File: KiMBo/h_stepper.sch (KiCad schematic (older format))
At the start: 24 parts, among them U18 TMC2130

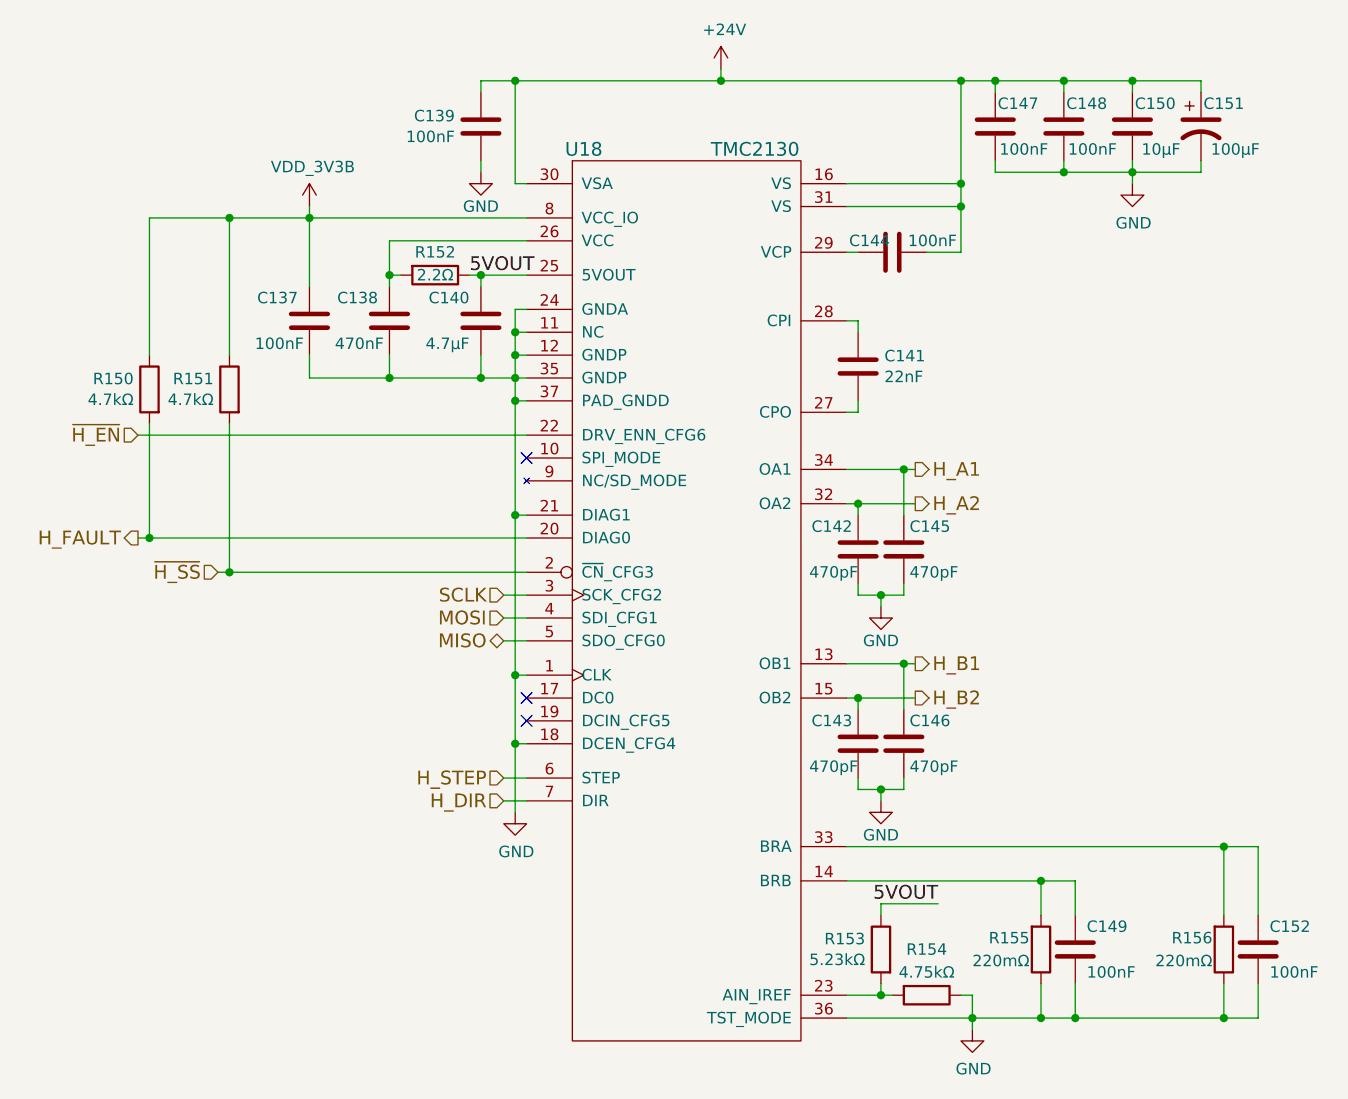
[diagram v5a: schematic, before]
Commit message: Add ferrite beads to the 5V and 3V pins at the SPI connectors
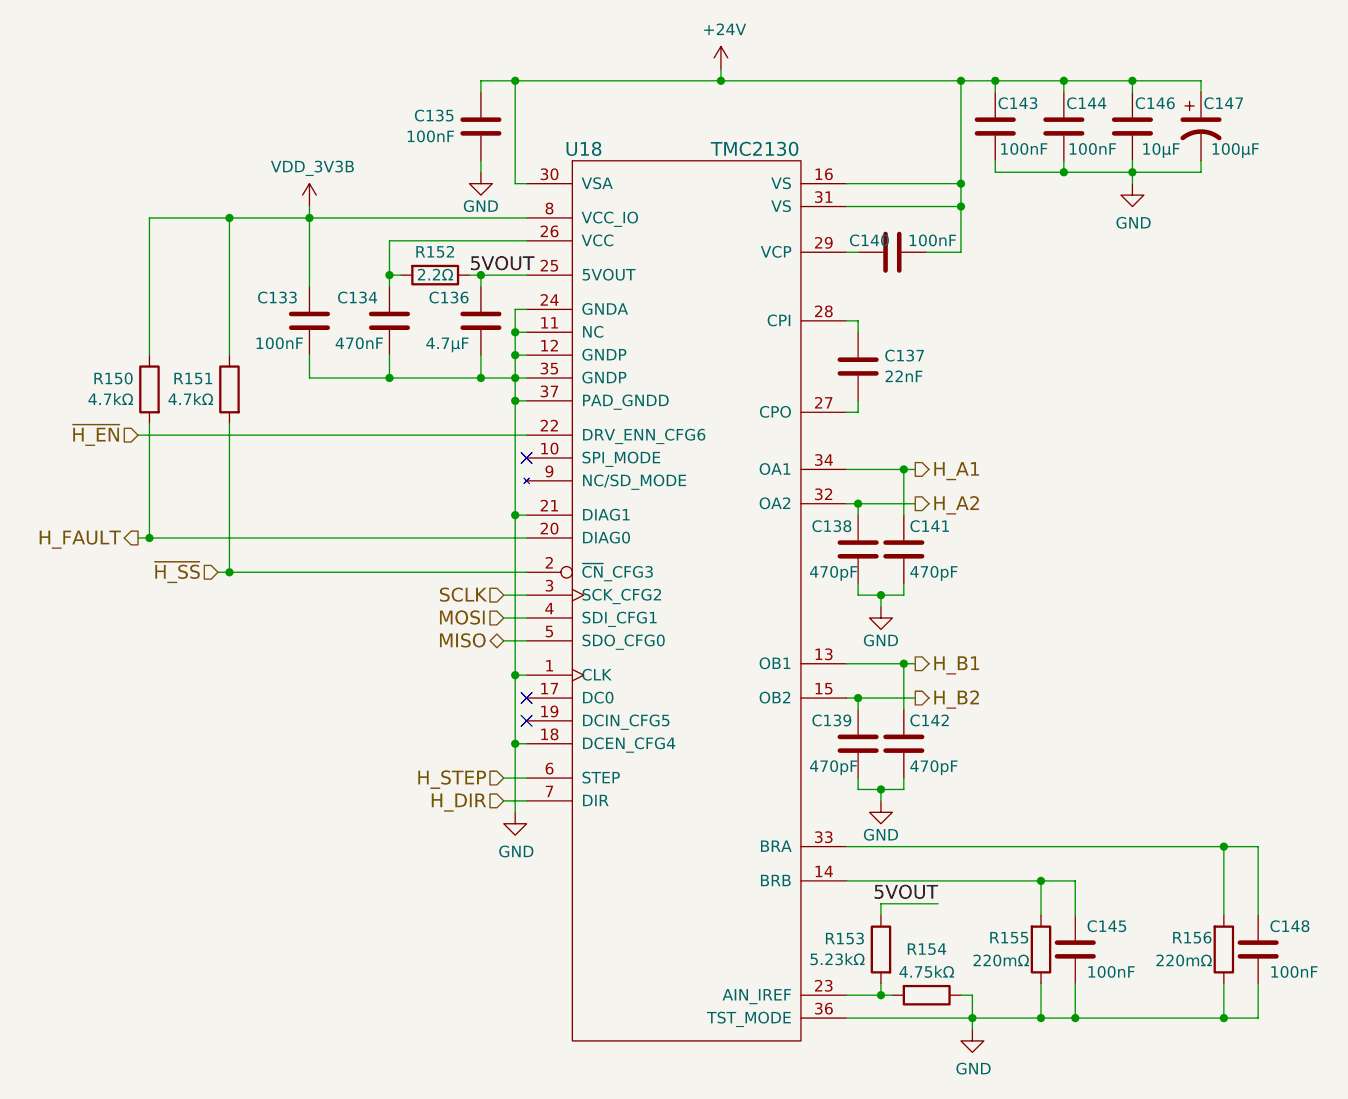
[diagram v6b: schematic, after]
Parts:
- renumbered C137 to C133, C138 to C134, C139 to C135, C140 to C136, C141 to C137, C142 to C138, C143 to C139, C144 to C140, C145 to C141, C146 to C142, C147 to C143, C148 to C144, C149 to C145, C150 to C146, C151 to C147, C152 to C148
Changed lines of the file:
@@
 MOSI
 $Comp
-L C C139
+L C C135
 U 1 1 5BA7E11E
 P 7300 3950
-F 0 "C139" H 7186 3904 50  0000 R CNN
+F 0 "C135" H 7186 3904 50  0000 R CNN
 F 1 "100nF" H 7186 3995 50  0000 R CNN
 F 2 "Capacitors_SMD:C_0603" H 7338 3800 50  0001 C CNN
@@
 $EndComp
 $Comp
-L C C144
+L C C140
 U 1 1 589B8C70
 P 9100 4500
-F 0 "C144" V 9050 4400 50  0000 C CNN
+F 0 "C140" V 9050 4400 50  0000 C CNN
 F 1 "100nF" V 9050 4675 50  0000 C CNN
 F 2 "Capacitors_SMD:C_0603" H 9138 4350 50  0001 C CNN
@@
 $EndComp
 $Comp
-L CP1 C151
+L CP1 C147
 U 1 1 589B8CBD
 P 10450 3950
-F 0 "C151" H 10550 4050 50  0000 C CNN
+F 0 "C147" H 10550 4050 50  0000 C CNN
 F 1 "100μF" H 10600 3850 50  0000 C CNN
 F 2 "Capacitors_SMD:c_elec_8x10" H 10450 3950 50  0001 C CNN
@@
 $EndComp
 $Comp
-L C C147
+L C C143
 U 1 1 5BA7E121
 P 9550 3950
-F 0 "C147" H 9450 4050 50  0000 C CNN
+F 0 "C143" H 9450 4050 50  0000 C CNN
 F 1 "100nF" H 9425 3850 50  0000 C CNN
 F 2 "Capacitors_SMD:C_0603" H 9588 3800 50  0001 C CNN
@@
 $EndComp
 $Comp
-L GND #PWR0205
+L GND #PWR0202
 U 1 1 5BA7E122
 P 7300 4150
-F 0 "#PWR0205" H 7300 3900 50  0001 C CNN
+F 0 "#PWR0202" H 7300 3900 50  0001 C CNN
 F 1 "GND" H 7300 4000 50  0000 C CNN
 F 2 "" H 7300 4150 50  0000 C CNN
@@
 $EndComp
 $Comp
-L C C148
+L C C144
 U 1 1 5BA7E123
 P 9850 3950
-F 0 "C148" H 9750 4050 50  0000 C CNN
+F 0 "C144" H 9750 4050 50  0000 C CNN
 F 1 "100nF" H 9725 3850 50  0000 C CNN
 F 2 "Capacitors_SMD:C_0603" H 9888 3800 50  0001 C CNN
@@
 $EndComp
 $Comp
-L GND #PWR0206
+L GND #PWR0203
 U 1 1 5BA7E124
 P 10150 4200
-F 0 "#PWR0206" H 10150 3950 50  0001 C CNN
+F 0 "#PWR0203" H 10150 3950 50  0001 C CNN
 F 1 "GND" H 10155 4027 50  0000 C CNN
 F 2 "" H 10150 4200 50  0000 C CNN
@@
 $EndComp
 $Comp
-L +24V #PWR0207
+L +24V #PWR0204
 U 1 1 589BEDE1
 P 8350 3700
-F 0 "#PWR0207" H 8350 3550 50  0001 C CNN
+F 0 "#PWR0204" H 8350 3550 50  0001 C CNN
 F 1 "+24V" H 8365 3873 50  0000 C CNN
 F 2 "" H 8350 3700 50  0000 C CNN
@@
 $EndComp
 $Comp
-L C C141
+L C C137
 U 1 1 5BA7E126
 P 8950 5000
-F 0 "C141" H 9065 5046 50  0000 L CNN
+F 0 "C137" H 9065 5046 50  0000 L CNN
 F 1 "22nF" H 9065 4955 50  0000 L CNN
 F 2 "Capacitors_SMD:C_0603" H 8988 4850 50  0001 C CNN
@@
 $EndComp
 $Comp
-L GND #PWR0208
+L GND #PWR0205
 U 1 1 589C2B70
 P 9450 7900
-F 0 "#PWR0208" H 9450 7650 50  0001 C CNN
+F 0 "#PWR0205" H 9450 7650 50  0001 C CNN
 F 1 "GND" H 9455 7727 50  0000 C CNN
 F 2 "" H 9450 7900 50  0000 C CNN
@@
 $EndComp
 $Comp
-L C C138
+L C C134
 U 1 1 5BA7E12C
 P 6900 4800
-F 0 "C138" H 6950 4900 50  0000 L CNN
+F 0 "C134" H 6950 4900 50  0000 L CNN
 F 1 "470nF" H 6925 4700 50  0000 L CNN
 F 2 "Capacitors_SMD:C_0603" H 6938 4650 50  0001 C CNN
@@
 NoConn ~ 7500 6550
 $Comp
-L GND #PWR0209
+L GND #PWR0206
 U 1 1 5BA7E12D
 P 7450 6950
-F 0 "#PWR0209" H 7450 6700 50  0001 C CNN
+F 0 "#PWR0206" H 7450 6700 50  0001 C CNN
 F 1 "GND" H 7455 6777 50  0000 C CNN
 F 2 "" H 7450 6950 50  0000 C CNN
@@
 $EndComp
 $Comp
-L C C149
+L C C145
 U 1 1 589CC9B9
 P 9900 7550
-F 0 "C149" H 9950 7650 50  0000 L CNN
+F 0 "C145" H 9950 7650 50  0000 L CNN
 F 1 "100nF" H 9950 7450 50  0000 L CNN
 F 2 "Capacitors_SMD:C_0603" H 9938 7400 50  0001 C CNN
@@
 NoConn ~ 7500 5400
 $Comp
-L C C140
+L C C136
 U 1 1 589C396E
 P 7300 4800
-F 0 "C140" H 7350 4900 50  0000 L CNN
+F 0 "C136" H 7350 4900 50  0000 L CNN
 F 1 "4.7μF" H 7350 4700 50  0000 L CNN
 F 2 "Capacitors_SMD:C_0603" H 7338 4650 50  0001 C CNN
@@
 $EndComp
 $Comp
-L C C152
+L C C148
 U 1 1 58AF169E
 P 10700 7550
-F 0 "C152" H 10750 7650 50  0000 L CNN
+F 0 "C148" H 10750 7650 50  0000 L CNN
 F 1 "100nF" H 10750 7450 50  0000 L CNN
 F 2 "Capacitors_SMD:C_0603" H 10738 7400 50  0001 C CNN
@@
 $EndComp
 $Comp
-L C C142
+L C C138
 U 1 1 58B19CCF
 P 8950 5800
-F 0 "C142" H 8975 5900 50  0000 L CNN
+F 0 "C138" H 8975 5900 50  0000 L CNN
 F 1 "470pF" H 8950 5700 50  0000 L CNN
 F 2 "Capacitors_SMD:C_0603" H 8988 5650 50  0001 C CNN
@@
 $EndComp
 $Comp
-L GND #PWR0210
+L GND #PWR0207
 U 1 1 5BA7E135
 P 9050 6050
-F 0 "#PWR0210" H 9050 5800 50  0001 C CNN
+F 0 "#PWR0207" H 9050 5800 50  0001 C CNN
 F 1 "GND" H 9050 5900 50  0000 C CNN
 F 2 "" H 9050 6050 50  0000 C CNN
@@
 $EndComp
 $Comp
-L C C145
+L C C141
 U 1 1 5BA7E136
 P 9150 5800
-F 0 "C145" H 9175 5900 50  0000 L CNN
+F 0 "C141" H 9175 5900 50  0000 L CNN
 F 1 "470pF" H 9175 5700 50  0000 L CNN
 F 2 "Capacitors_SMD:C_0603" H 9188 5650 50  0001 C CNN
@@
 $EndComp
 $Comp
-L C C143
+L C C139
 U 1 1 5BA7E137
 P 8950 6650
-F 0 "C143" H 8975 6750 50  0000 L CNN
+F 0 "C139" H 8975 6750 50  0000 L CNN
 F 1 "470pF" H 8950 6550 50  0000 L CNN
 F 2 "Capacitors_SMD:C_0603" H 8988 6500 50  0001 C CNN
@@
 $EndComp
 $Comp
-L GND #PWR0211
+L GND #PWR0208
 U 1 1 5BA7E138
 P 9050 6900
-F 0 "#PWR0211" H 9050 6650 50  0001 C CNN
+F 0 "#PWR0208" H 9050 6650 50  0001 C CNN
 F 1 "GND" H 9050 6750 50  0000 C CNN
 F 2 "" H 9050 6900 50  0000 C CNN
@@
 $EndComp
 $Comp
-L C C146
+L C C142
 U 1 1 5BA7E139
 P 9150 6650
-F 0 "C146" H 9175 6750 50  0000 L CNN
+F 0 "C142" H 9175 6750 50  0000 L CNN
 F 1 "470pF" H 9175 6550 50  0000 L CNN
 F 2 "Capacitors_SMD:C_0603" H 9188 6500 50  0001 C CNN
@@
 	8950 6850 8950 6800
 $Comp
-L C C150
+L C C146
 U 1 1 5BA7E13A
 P 10150 3950
-F 0 "C150" H 10050 4050 50  0000 C CNN
+F 0 "C146" H 10050 4050 50  0000 C CNN
 F 1 "10μF" H 10025 3850 50  0000 C CNN
 F 2 "Capacitors_SMD:C_0805" H 10188 3800 50  0001 C CNN
@@
 	5850 4350 7500 4350
 $Comp
-L VDD_3V3B #PWR0212
+L VDD_3V3B #PWR0209
 U 1 1 5A2FEA7A
 P 6550 4300
-F 0 "#PWR0212" H 6550 4150 50  0001 C CNN
+F 0 "#PWR0209" H 6550 4150 50  0001 C CNN
 F 1 "VDD_3V3B" H 6565 4473 50  0000 C CNN
 F 2 "" H 6550 4300 50  0000 C CNN
@@
 $EndComp
 $Comp
-L C C137
+L C C133
 U 1 1 5A897FB1
 P 6550 4800
-F 0 "C137" H 6600 4900 50  0000 L CNN
+F 0 "C133" H 6600 4900 50  0000 L CNN
 F 1 "100nF" H 6575 4700 50  0000 L CNN
 F 2 "Capacitors_SMD:C_0603" H 6588 4650 50  0001 C CNN

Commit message: Complete SPI, ADC, and Endstop header layout/position, add zone around the SiP
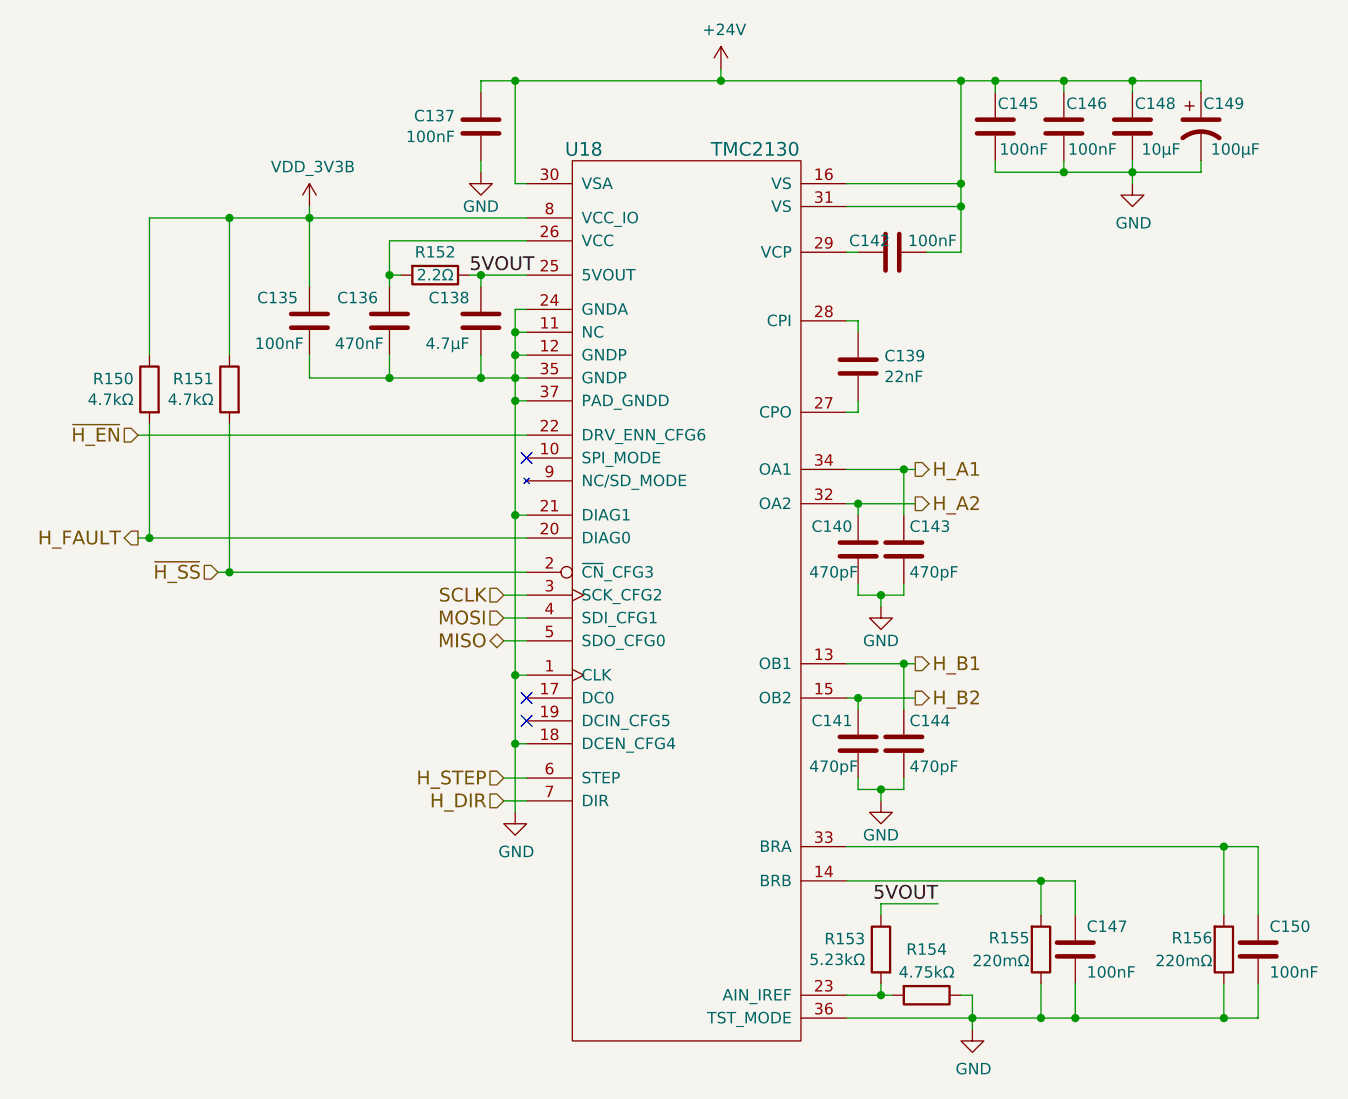
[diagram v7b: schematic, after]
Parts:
- renumbered C133 to C135, C134 to C136, C135 to C137, C136 to C138, C137 to C139, C138 to C140, C139 to C141, C140 to C142, C141 to C143, C142 to C144, C143 to C145, C144 to C146, C145 to C147, C146 to C148, C147 to C149, C148 to C150
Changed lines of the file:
@@
 MOSI
 $Comp
-L C C135
+L C C137
 U 1 1 5BA7E11E
 P 7300 3950
-F 0 "C135" H 7186 3904 50  0000 R CNN
+F 0 "C137" H 7186 3904 50  0000 R CNN
 F 1 "100nF" H 7186 3995 50  0000 R CNN
 F 2 "Capacitors_SMD:C_0603" H 7338 3800 50  0001 C CNN
@@
 $EndComp
 $Comp
-L C C140
+L C C142
 U 1 1 589B8C70
 P 9100 4500
-F 0 "C140" V 9050 4400 50  0000 C CNN
+F 0 "C142" V 9050 4400 50  0000 C CNN
 F 1 "100nF" V 9050 4675 50  0000 C CNN
 F 2 "Capacitors_SMD:C_0603" H 9138 4350 50  0001 C CNN
@@
 $EndComp
 $Comp
-L CP1 C147
+L CP1 C149
 U 1 1 589B8CBD
 P 10450 3950
-F 0 "C147" H 10550 4050 50  0000 C CNN
+F 0 "C149" H 10550 4050 50  0000 C CNN
 F 1 "100μF" H 10600 3850 50  0000 C CNN
 F 2 "Capacitors_SMD:c_elec_8x10" H 10450 3950 50  0001 C CNN
@@
 $EndComp
 $Comp
-L C C143
+L C C145
 U 1 1 5BA7E121
 P 9550 3950
-F 0 "C143" H 9450 4050 50  0000 C CNN
+F 0 "C145" H 9450 4050 50  0000 C CNN
 F 1 "100nF" H 9425 3850 50  0000 C CNN
 F 2 "Capacitors_SMD:C_0603" H 9588 3800 50  0001 C CNN
@@
 $EndComp
 $Comp
-L GND #PWR0202
+L GND #PWR0204
 U 1 1 5BA7E122
 P 7300 4150
-F 0 "#PWR0202" H 7300 3900 50  0001 C CNN
+F 0 "#PWR0204" H 7300 3900 50  0001 C CNN
 F 1 "GND" H 7300 4000 50  0000 C CNN
 F 2 "" H 7300 4150 50  0000 C CNN
@@
 $EndComp
 $Comp
-L C C144
+L C C146
 U 1 1 5BA7E123
 P 9850 3950
-F 0 "C144" H 9750 4050 50  0000 C CNN
+F 0 "C146" H 9750 4050 50  0000 C CNN
 F 1 "100nF" H 9725 3850 50  0000 C CNN
 F 2 "Capacitors_SMD:C_0603" H 9888 3800 50  0001 C CNN
@@
 $EndComp
 $Comp
-L GND #PWR0203
+L GND #PWR0205
 U 1 1 5BA7E124
 P 10150 4200
-F 0 "#PWR0203" H 10150 3950 50  0001 C CNN
+F 0 "#PWR0205" H 10150 3950 50  0001 C CNN
 F 1 "GND" H 10155 4027 50  0000 C CNN
 F 2 "" H 10150 4200 50  0000 C CNN
@@
 $EndComp
 $Comp
-L +24V #PWR0204
+L +24V #PWR0206
 U 1 1 589BEDE1
 P 8350 3700
-F 0 "#PWR0204" H 8350 3550 50  0001 C CNN
+F 0 "#PWR0206" H 8350 3550 50  0001 C CNN
 F 1 "+24V" H 8365 3873 50  0000 C CNN
 F 2 "" H 8350 3700 50  0000 C CNN
@@
 $EndComp
 $Comp
-L C C137
+L C C139
 U 1 1 5BA7E126
 P 8950 5000
-F 0 "C137" H 9065 5046 50  0000 L CNN
+F 0 "C139" H 9065 5046 50  0000 L CNN
 F 1 "22nF" H 9065 4955 50  0000 L CNN
 F 2 "Capacitors_SMD:C_0603" H 8988 4850 50  0001 C CNN
@@
 $EndComp
 $Comp
-L GND #PWR0205
+L GND #PWR0207
 U 1 1 589C2B70
 P 9450 7900
-F 0 "#PWR0205" H 9450 7650 50  0001 C CNN
+F 0 "#PWR0207" H 9450 7650 50  0001 C CNN
 F 1 "GND" H 9455 7727 50  0000 C CNN
 F 2 "" H 9450 7900 50  0000 C CNN
@@
 $EndComp
 $Comp
-L C C134
+L C C136
 U 1 1 5BA7E12C
 P 6900 4800
-F 0 "C134" H 6950 4900 50  0000 L CNN
+F 0 "C136" H 6950 4900 50  0000 L CNN
 F 1 "470nF" H 6925 4700 50  0000 L CNN
 F 2 "Capacitors_SMD:C_0603" H 6938 4650 50  0001 C CNN
@@
 NoConn ~ 7500 6550
 $Comp
-L GND #PWR0206
+L GND #PWR0208
 U 1 1 5BA7E12D
 P 7450 6950
-F 0 "#PWR0206" H 7450 6700 50  0001 C CNN
+F 0 "#PWR0208" H 7450 6700 50  0001 C CNN
 F 1 "GND" H 7455 6777 50  0000 C CNN
 F 2 "" H 7450 6950 50  0000 C CNN
@@
 $EndComp
 $Comp
-L C C145
+L C C147
 U 1 1 589CC9B9
 P 9900 7550
-F 0 "C145" H 9950 7650 50  0000 L CNN
+F 0 "C147" H 9950 7650 50  0000 L CNN
 F 1 "100nF" H 9950 7450 50  0000 L CNN
 F 2 "Capacitors_SMD:C_0603" H 9938 7400 50  0001 C CNN
@@
 NoConn ~ 7500 5400
 $Comp
-L C C136
+L C C138
 U 1 1 589C396E
 P 7300 4800
-F 0 "C136" H 7350 4900 50  0000 L CNN
+F 0 "C138" H 7350 4900 50  0000 L CNN
 F 1 "4.7μF" H 7350 4700 50  0000 L CNN
 F 2 "Capacitors_SMD:C_0603" H 7338 4650 50  0001 C CNN
@@
 $EndComp
 $Comp
-L C C148
+L C C150
 U 1 1 58AF169E
 P 10700 7550
-F 0 "C148" H 10750 7650 50  0000 L CNN
+F 0 "C150" H 10750 7650 50  0000 L CNN
 F 1 "100nF" H 10750 7450 50  0000 L CNN
 F 2 "Capacitors_SMD:C_0603" H 10738 7400 50  0001 C CNN
@@
 $EndComp
 $Comp
-L C C138
+L C C140
 U 1 1 58B19CCF
 P 8950 5800
-F 0 "C138" H 8975 5900 50  0000 L CNN
+F 0 "C140" H 8975 5900 50  0000 L CNN
 F 1 "470pF" H 8950 5700 50  0000 L CNN
 F 2 "Capacitors_SMD:C_0603" H 8988 5650 50  0001 C CNN
@@
 $EndComp
 $Comp
-L GND #PWR0207
+L GND #PWR0209
 U 1 1 5BA7E135
 P 9050 6050
-F 0 "#PWR0207" H 9050 5800 50  0001 C CNN
+F 0 "#PWR0209" H 9050 5800 50  0001 C CNN
 F 1 "GND" H 9050 5900 50  0000 C CNN
 F 2 "" H 9050 6050 50  0000 C CNN
@@
 $EndComp
 $Comp
-L C C141
+L C C143
 U 1 1 5BA7E136
 P 9150 5800
-F 0 "C141" H 9175 5900 50  0000 L CNN
+F 0 "C143" H 9175 5900 50  0000 L CNN
 F 1 "470pF" H 9175 5700 50  0000 L CNN
 F 2 "Capacitors_SMD:C_0603" H 9188 5650 50  0001 C CNN
@@
 $EndComp
 $Comp
-L C C139
+L C C141
 U 1 1 5BA7E137
 P 8950 6650
-F 0 "C139" H 8975 6750 50  0000 L CNN
+F 0 "C141" H 8975 6750 50  0000 L CNN
 F 1 "470pF" H 8950 6550 50  0000 L CNN
 F 2 "Capacitors_SMD:C_0603" H 8988 6500 50  0001 C CNN
@@
 $EndComp
 $Comp
-L GND #PWR0208
+L GND #PWR0210
 U 1 1 5BA7E138
 P 9050 6900
-F 0 "#PWR0208" H 9050 6650 50  0001 C CNN
+F 0 "#PWR0210" H 9050 6650 50  0001 C CNN
 F 1 "GND" H 9050 6750 50  0000 C CNN
 F 2 "" H 9050 6900 50  0000 C CNN
@@
 $EndComp
 $Comp
-L C C142
+L C C144
 U 1 1 5BA7E139
 P 9150 6650
-F 0 "C142" H 9175 6750 50  0000 L CNN
+F 0 "C144" H 9175 6750 50  0000 L CNN
 F 1 "470pF" H 9175 6550 50  0000 L CNN
 F 2 "Capacitors_SMD:C_0603" H 9188 6500 50  0001 C CNN
@@
 	8950 6850 8950 6800
 $Comp
-L C C146
+L C C148
 U 1 1 5BA7E13A
 P 10150 3950
-F 0 "C146" H 10050 4050 50  0000 C CNN
+F 0 "C148" H 10050 4050 50  0000 C CNN
 F 1 "10μF" H 10025 3850 50  0000 C CNN
 F 2 "Capacitors_SMD:C_0805" H 10188 3800 50  0001 C CNN
@@
 	5850 4350 7500 4350
 $Comp
-L VDD_3V3B #PWR0209
+L VDD_3V3B #PWR0211
 U 1 1 5A2FEA7A
 P 6550 4300
-F 0 "#PWR0209" H 6550 4150 50  0001 C CNN
+F 0 "#PWR0211" H 6550 4150 50  0001 C CNN
 F 1 "VDD_3V3B" H 6565 4473 50  0000 C CNN
 F 2 "" H 6550 4300 50  0000 C CNN
@@
 $EndComp
 $Comp
-L C C133
+L C C135
 U 1 1 5A897FB1
 P 6550 4800
-F 0 "C133" H 6600 4900 50  0000 L CNN
+F 0 "C135" H 6600 4900 50  0000 L CNN
 F 1 "100nF" H 6575 4700 50  0000 L CNN
 F 2 "Capacitors_SMD:C_0603" H 6588 4650 50  0001 C CNN
